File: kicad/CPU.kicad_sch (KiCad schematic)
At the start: 21 parts, among them SW1 SW_Push, U5 STM32F303CBTx, X1 8 MHz

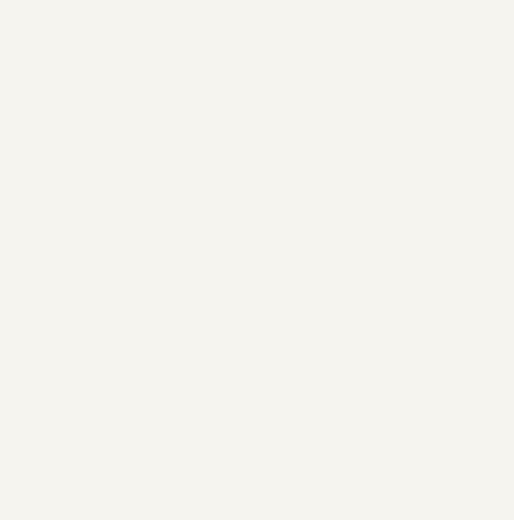
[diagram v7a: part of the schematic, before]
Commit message: [ltspice] added MC34063 simulation model
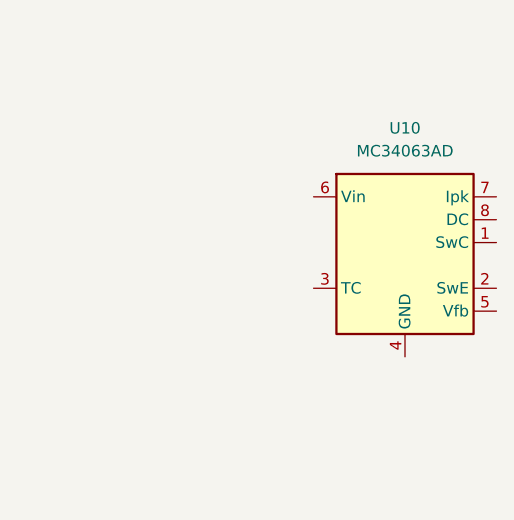
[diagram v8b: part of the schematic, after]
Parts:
- added U10: MC34063AD, Package_SO:SOIC-8_3.9x4.9mm_P1.27mm, symbol Regulator_Switching:MC34063AD
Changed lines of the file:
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@@
+    )
+  )
+  (symbol (lib_id "Regulator_Switching:MC34063AD") (at 213.36 39.37 0) (unit 1)
+    (in_bom yes) (on_board yes) (dnp no) (fields_autoplaced)
+    (property "Reference" "U10" (at 213.36 26.67 0)
+      (effects (font (size 1.27 1.27)))
+    )
+    (property "Value" "MC34063AD" (at 213.36 29.21 0)
+      (effects (font (size 1.27 1.27)))
+    )
+    (property "Footprint" "Package_SO:SOIC-8_3.9x4.9mm_P1.27mm" (at 214.63 50.8 0)
+      (effects (font (size 1.27 1.27)) (justify left) hide)
+    )
+    (property "Datasheet" "http://www.onsemi.com/pub_link/Collateral/MC34063A-D.PDF" (at 226.06 41.91 0)
+      (effects (font (size 1.27 1.27)) hide)
+    )
+    (pin "5")
+    (pin "7")
+    (pin "6")
+    (pin "4")
+    (pin "3")
+    (pin "1")
+    (pin "8")
+    (pin "2")
+    (instances
+      (project "bldc_project"
+        (path "/91e2f46a-700b-4d7a-a06a-22469f63223f/7eb1e86b-8a48-408f-b231-0c52f4ea1971"
+          (reference "U10") (unit 1)
+        )
+      )
     )
   )
